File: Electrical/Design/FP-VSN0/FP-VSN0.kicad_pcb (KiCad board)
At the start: 2 copper layers, 104.4 x 104.4 mm, 21 parts

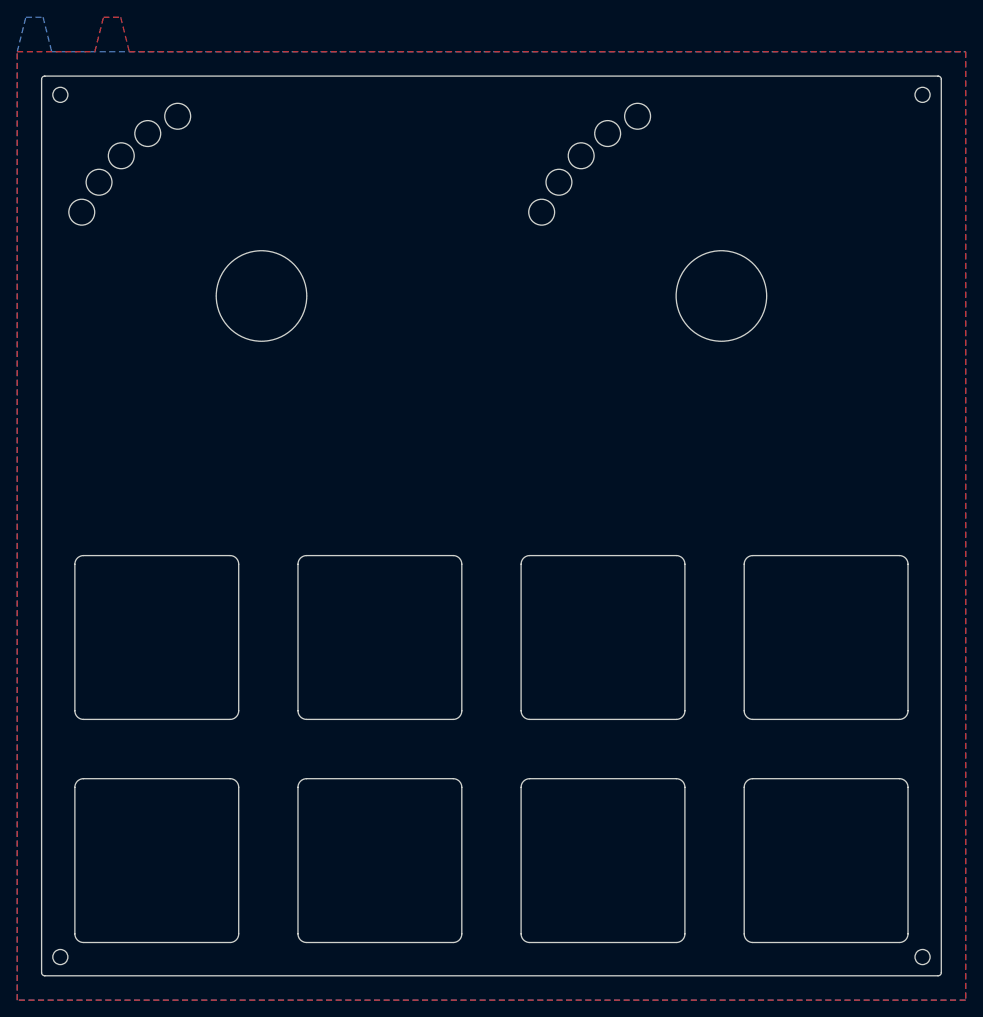
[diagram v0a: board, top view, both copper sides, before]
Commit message: SUKU frontpanel hatch pattern updated, outline updated, silk screen updated
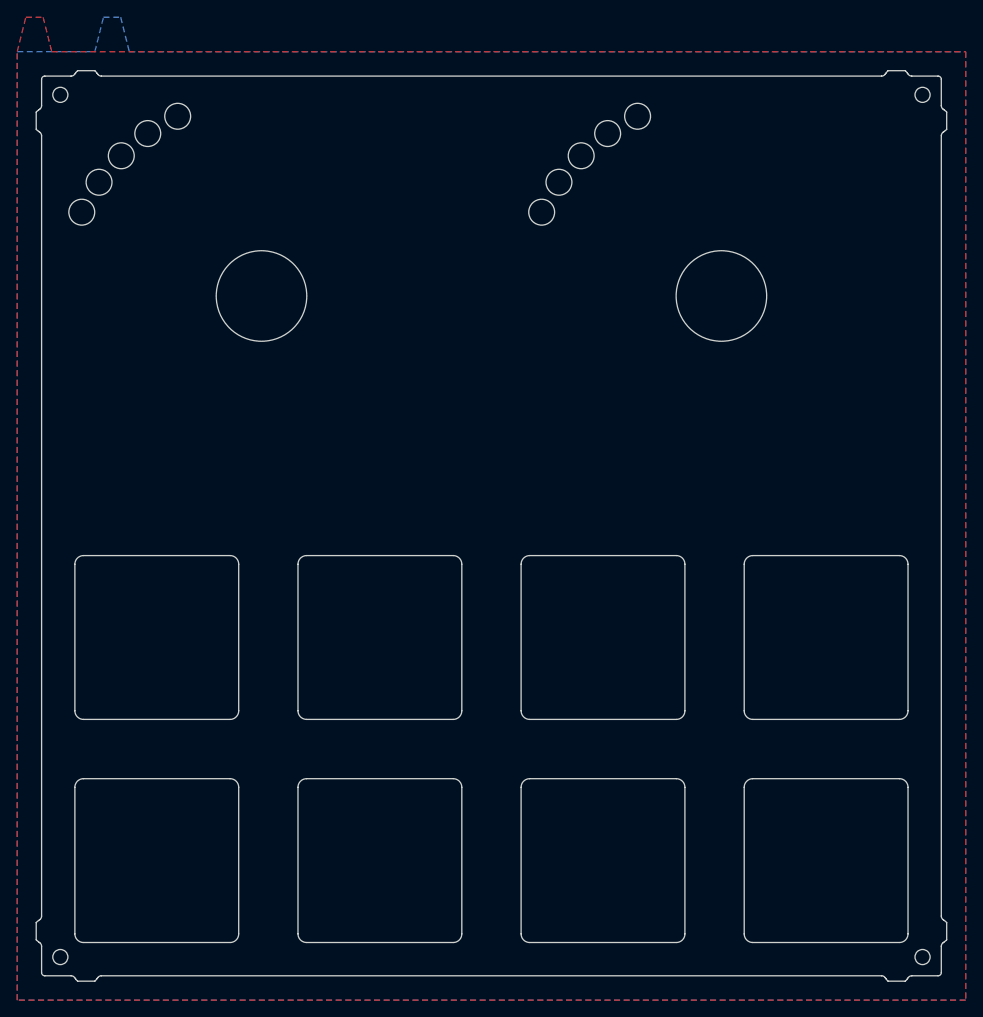
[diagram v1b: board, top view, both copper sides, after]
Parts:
- added H522: Outline, suku_basics:OSHWA, B.Cu at (115.0, 95.0)
- H504: footprint suku_basics:FP_OUTLINE -> suku_basics:FP_OUTLINE_2
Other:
- board size 104.4 x 104.4 mm -> 105.6 x 105.6 mm
- board text added: "Hello Hacker!"
- board text added: "JLCJLCJLCJLC ${PROJECTNAME} ${HASH} ${DATE}"
- board text added: "My name is:"
- board text removed: "${PROJECTNAME} ${HASH} ${DATE}"
- board text removed: "Default Routing Grid: 0,2500 mm Analog Routing Grid: 0,1270 mm LED Routing Grid: 0,6350 mm"
